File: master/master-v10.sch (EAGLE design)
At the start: 44 parts

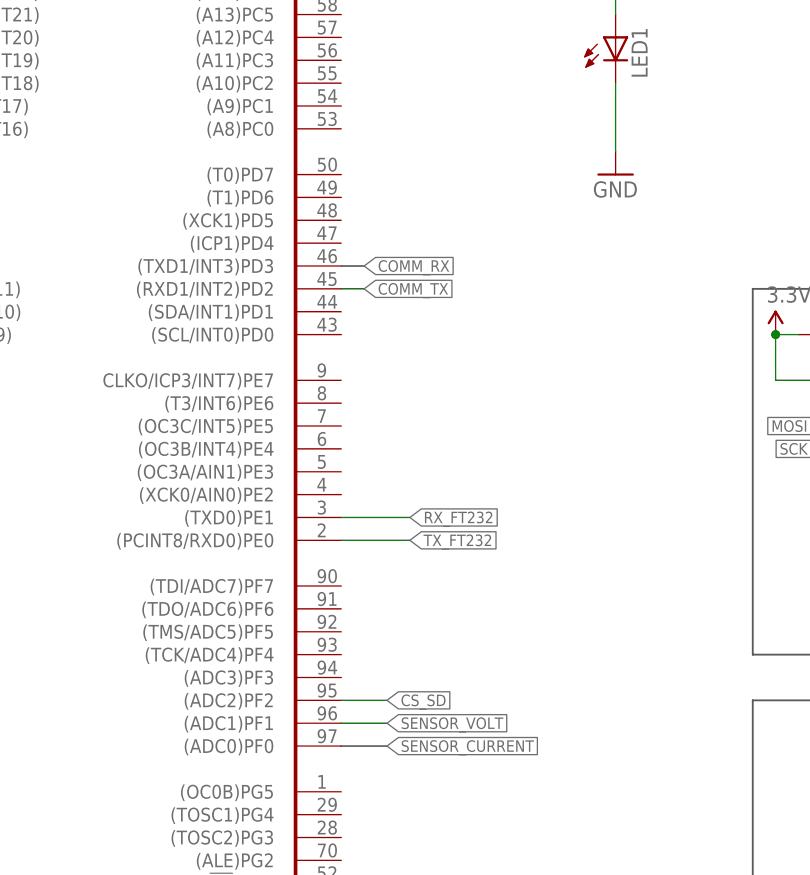
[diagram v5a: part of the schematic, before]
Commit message: algunos arreglos
Solo falta pistas del sensor de corriente y algunas tierras
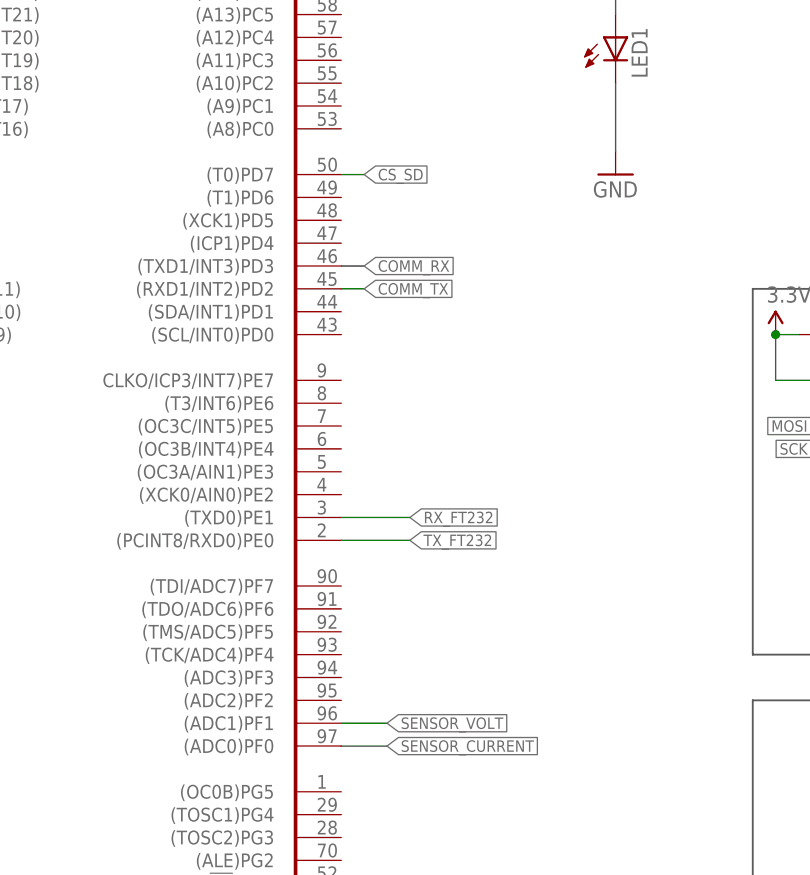
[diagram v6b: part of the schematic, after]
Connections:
- net CS_SD: now also ATMEGA1280.(T0)PD7; no longer ATMEGA1280.(ADC2)PF2
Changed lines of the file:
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@@
 <net name="CS_SD" class="0">
-<segment>
-<pinref part="ATMEGA1280" gate="G$1" pin="(ADC2)PF2"/>
-<wire x1="236.22" y1="114.3" x2="241.3" y2="114.3" width="0.1524" layer="91"/>
-<label x="241.3" y="114.3" size="1.27" layer="95" xref="yes"/>
-</segment>
 <segment>
 <pinref part="MICROSD" gate="G$1" pin="CS"/>
@@
 <label x="325.12" y="93.98" size="1.778" layer="95"/>
 </segment>
+<segment>
+<pinref part="ATMEGA1280" gate="G$1" pin="(T0)PD7"/>
+<wire x1="236.22" y1="172.72" x2="238.76" y2="172.72" width="0.1524" layer="91"/>
+<label x="238.76" y="172.72" size="1.27" layer="95" xref="yes"/>
+</segment>
 </net>

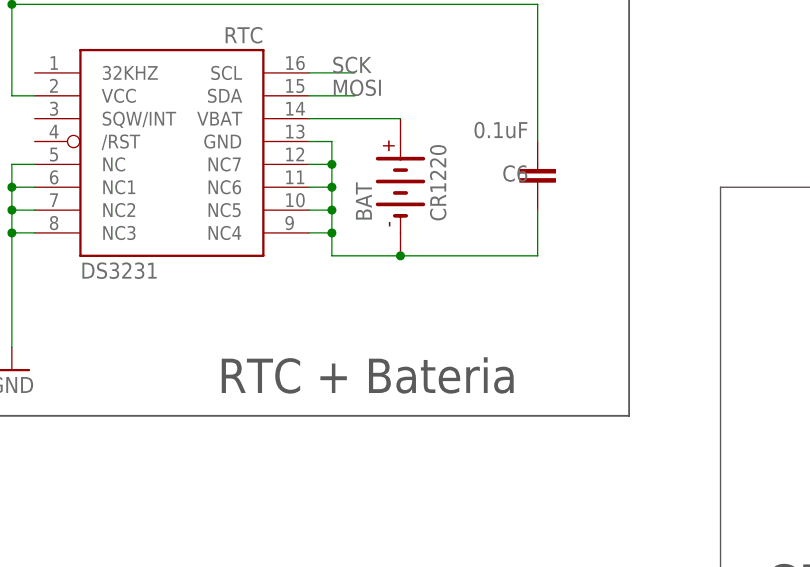
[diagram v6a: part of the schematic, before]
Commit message: Corregdas pistas, corregido error en la pila del RTC
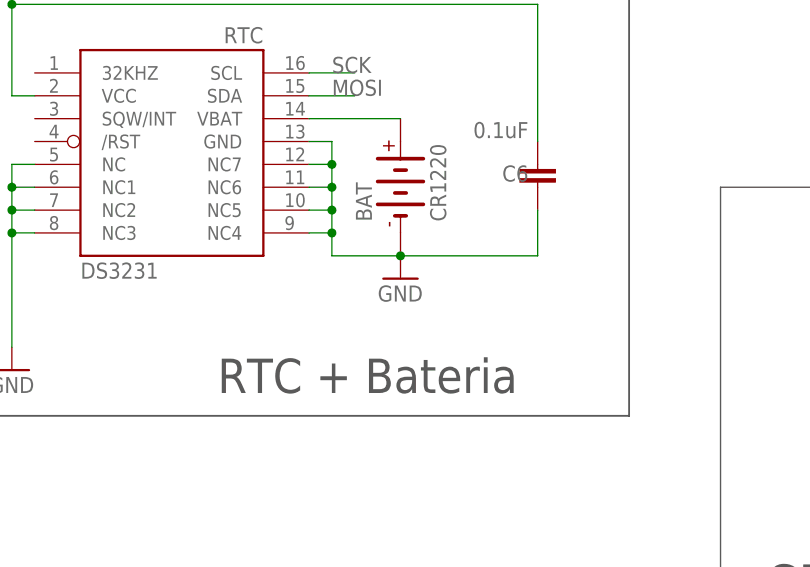
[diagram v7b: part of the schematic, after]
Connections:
- removed net N$9: BAT.-, C6.2, RTC.GND, RTC.NC4, RTC.NC5, RTC.NC6, RTC.NC7
- net GND: now also BAT.-, C6.2, RTC.GND, RTC.NC4, RTC.NC5, RTC.NC6, RTC.NC7

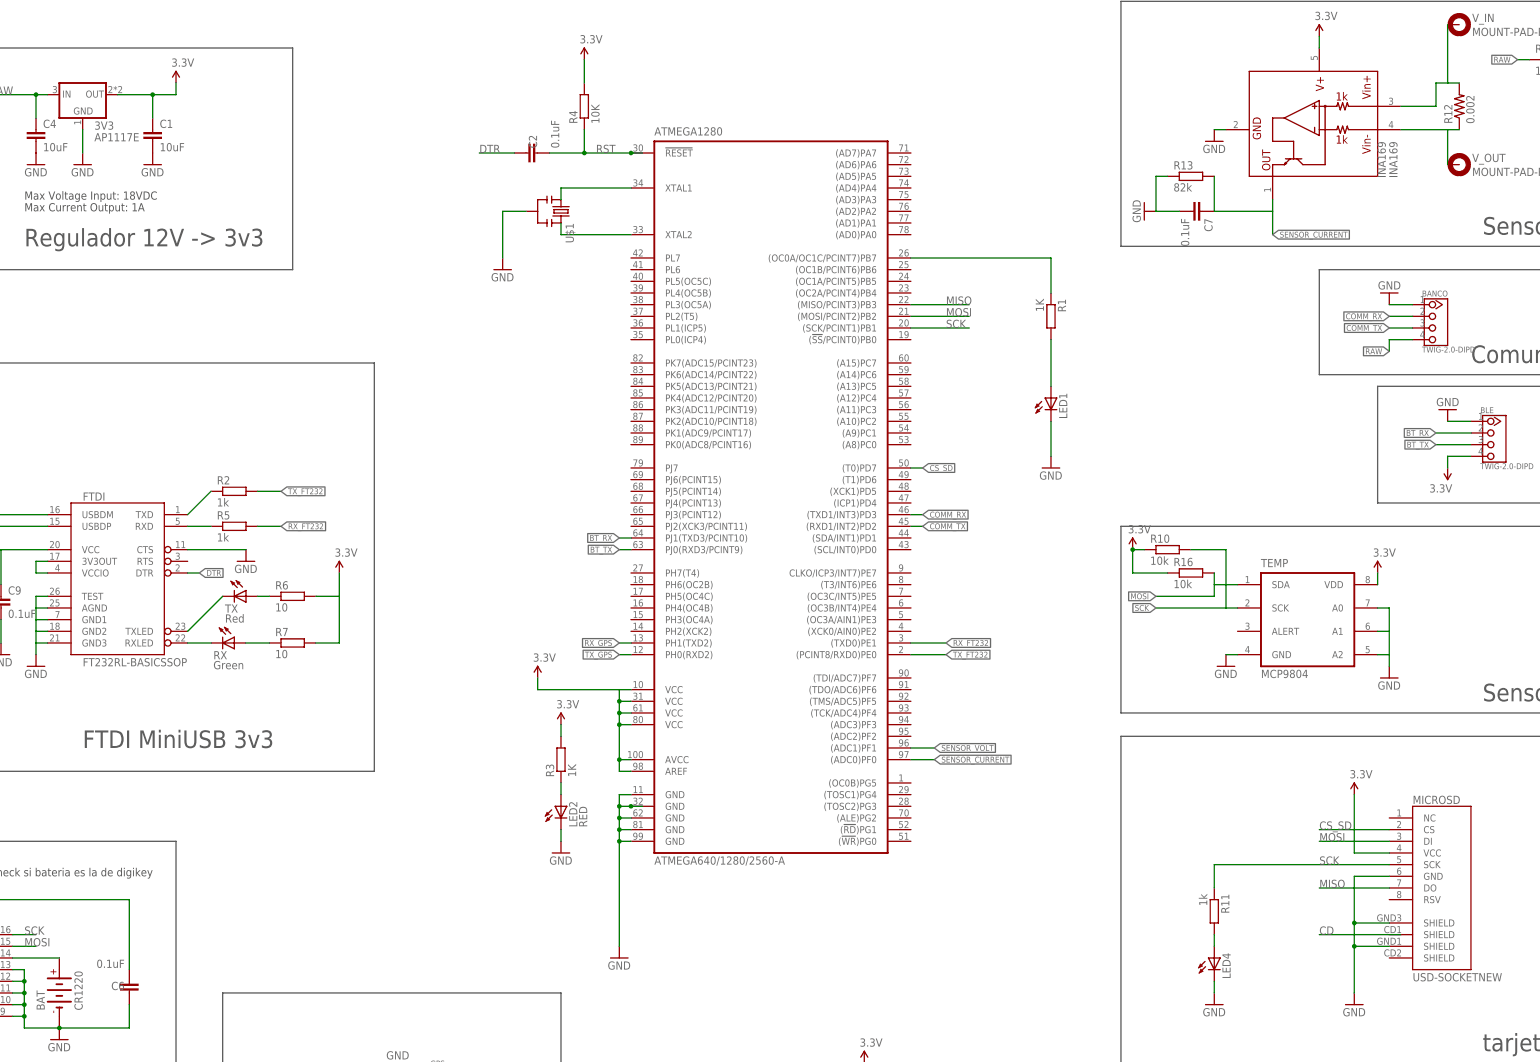
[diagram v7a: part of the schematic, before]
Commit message: Ajustado silk Screen
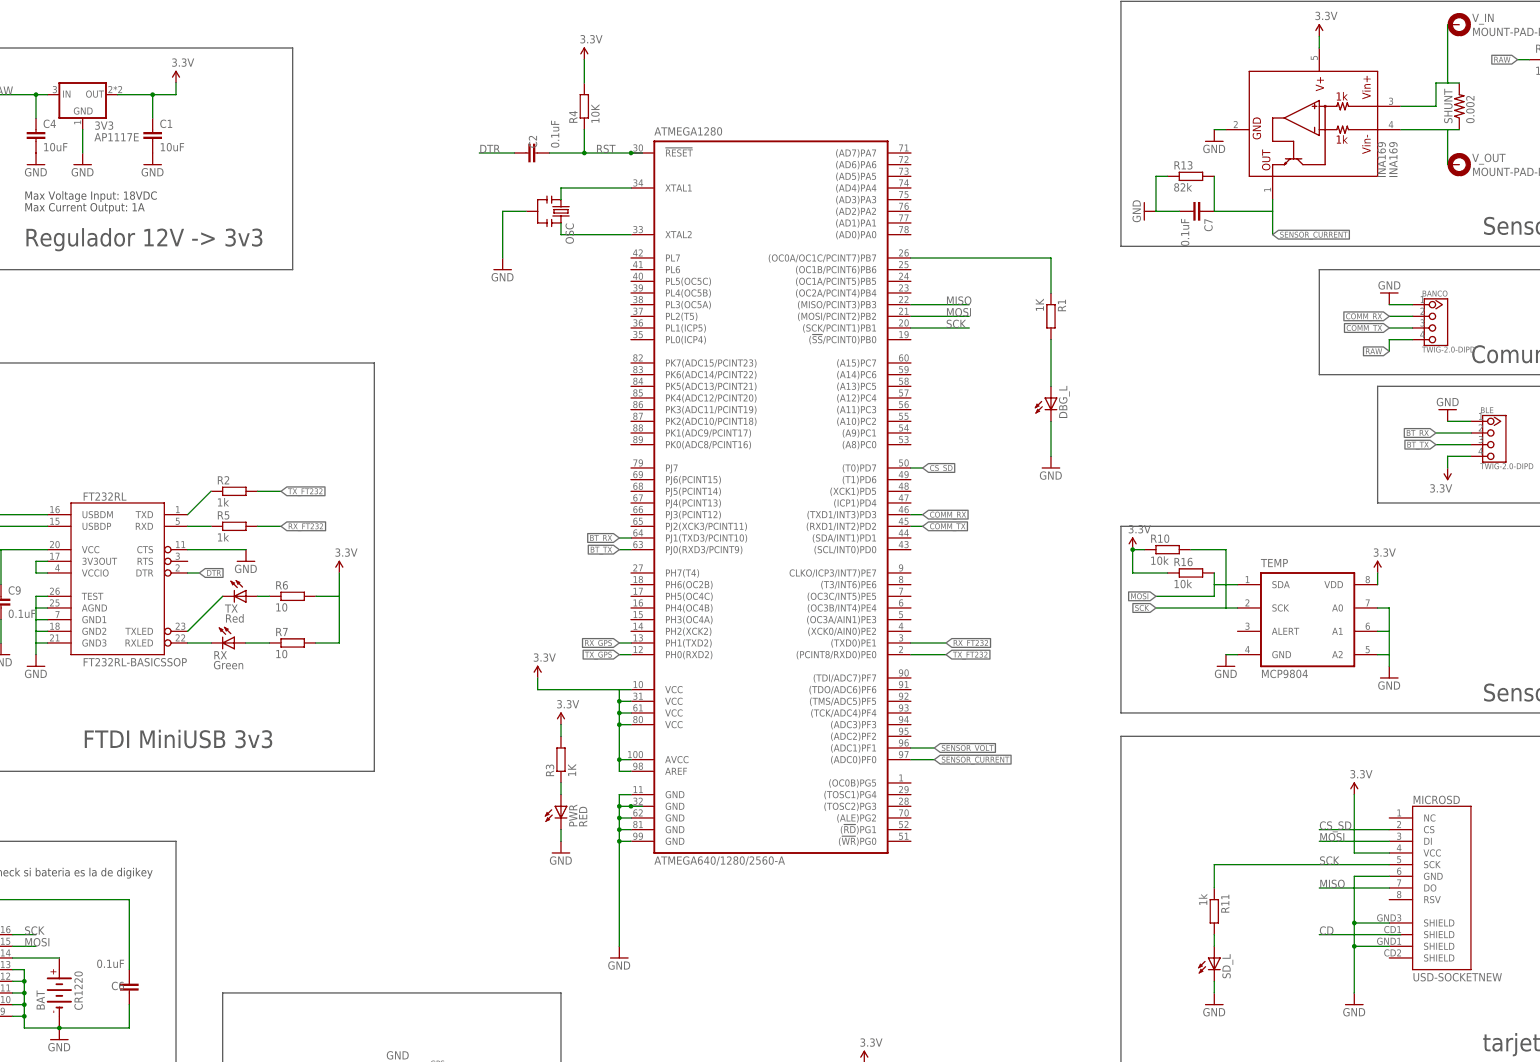
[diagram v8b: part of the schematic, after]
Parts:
- renumbered FTDI to FT232RL, LED1 to DBG_L, LED2 to PWR, LED4 to SD_L, R12 to SHUNT, U$1 to OSC
